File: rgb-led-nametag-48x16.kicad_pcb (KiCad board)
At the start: 4 copper layers, 84 x 28.8 mm, 109 parts, among them J1 USB_C_Receptacle_USB2.0, Q1 CJ3139K, Q10 CJ3139K, Q11 CJ3139K, Q12 CJ3139K, Q13 CJ3139K, Q14 CJ3139K, Q15 CJ3139K, Q16 CJ3139K, Q2 CJ3139K, Q3 CJ3139K, Q4 CJ3139K, Q5 CJ3139K, Q6 CJ3139K, Q7 CJ3139K, Q8 CJ3139K, Q9 CJ3139K, U1 led-panel-16x16, U10 74HC595, U11 74HC595, U12 74HC595, U13 74HC595, U14 74HC595, U15 74HC595, U16 led-panel-16x16, U17 74HC595, U18 74HC595, U19 74HC595, U2 74HC595, U20 74HC595, U21 74HC595, U22 74HC595, U23 74HC595, U24 ESP32-PICO-D4, U3 74HC595, U4 74HC595, U5 74HC595, U6 74HC595, U7 74HC595, U8 74HC595, U9 led-panel-16x16

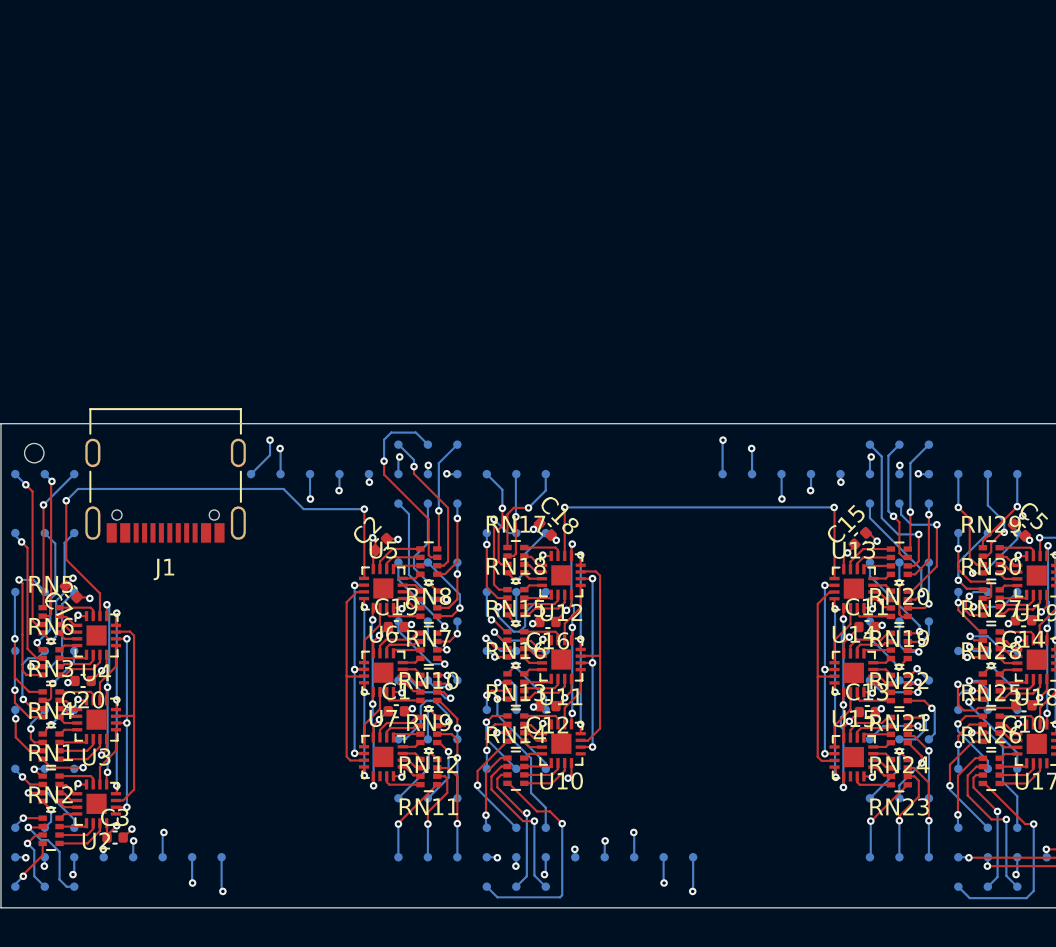
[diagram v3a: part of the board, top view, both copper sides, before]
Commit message: Add multiplexing MCU and USB
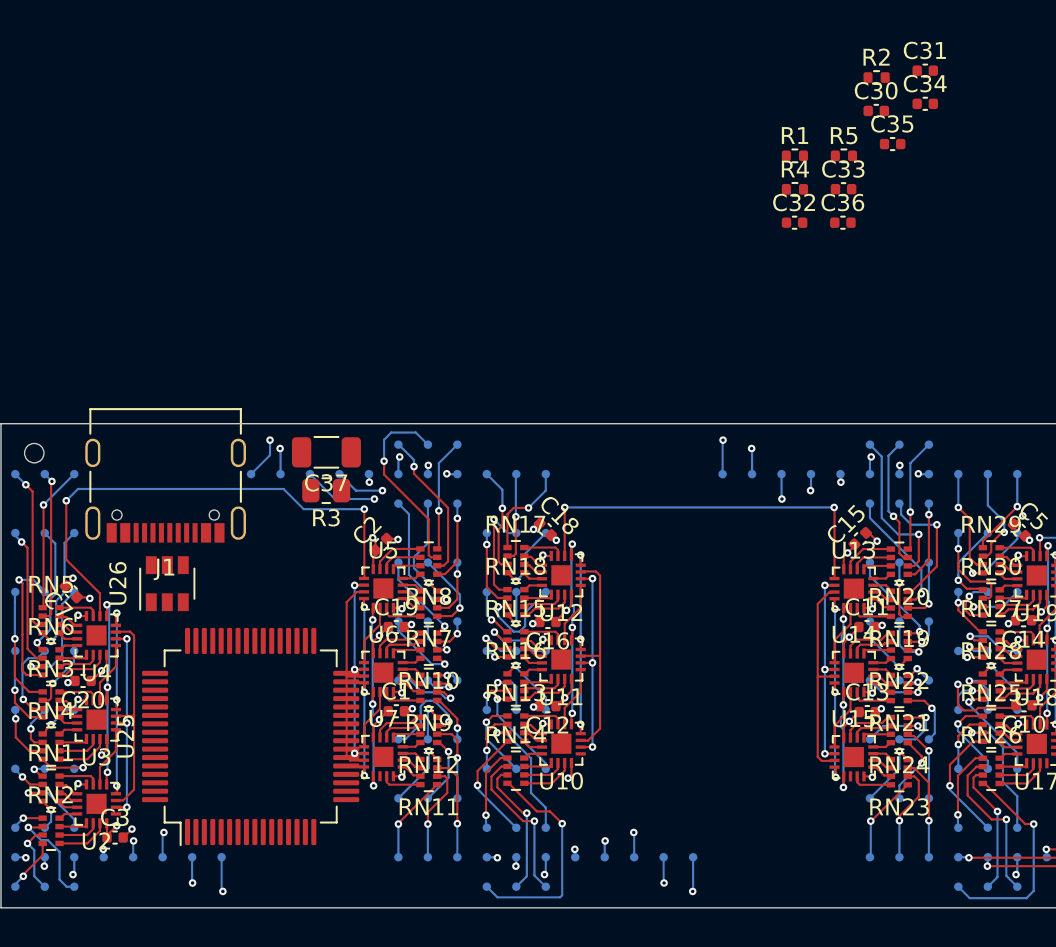
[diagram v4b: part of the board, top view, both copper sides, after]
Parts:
- added C30: 100nF, Capacitor_SMD:C_0402_1005Metric, F.Cu at (143.4, 76.2)
- added C31: 4.7uF, Capacitor_SMD:C_0402_1005Metric, F.Cu at (146.3, 73.8)
- added C32: 100nF, Capacitor_SMD:C_0402_1005Metric, F.Cu at (138.6, 82.8)
- added C33: 100nF, Capacitor_SMD:C_0402_1005Metric, F.Cu at (141.5, 80.8)
- added C34: 100nF, Capacitor_SMD:C_0402_1005Metric, F.Cu at (146.3, 75.7)
- added C35: 100nF, Capacitor_SMD:C_0402_1005Metric, F.Cu at (144.4, 78.1)
- added C36: 100nF, Capacitor_SMD:C_0402_1005Metric, F.Cu at (141.4, 82.8)
- added C37: 1nF, Capacitor_SMD:C_1206_3216Metric, F.Cu at (110.8, 96.4)
- added R1: 100k, Resistor_SMD:R_0402_1005Metric, F.Cu at (138.6, 78.8)
- added R2: 100k, Resistor_SMD:R_0402_1005Metric, F.Cu at (143.4, 74.2)
- added R3: 200k, Resistor_SMD:R_0805_2012Metric, F.Cu at (110.7, 98.7)
- added R4: 5.1k, Resistor_SMD:R_0402_1005Metric, F.Cu at (138.6, 80.8)
- added R5: 5.1k, Resistor_SMD:R_0402_1005Metric, F.Cu at (141.5, 78.8)
- added U25: STM32F722RETx, Package_QFP:LQFP-64_10x10mm_P0.5mm, F.Cu at (106.2, 113.3)
- added U26: SRV05-4, Package_TO_SOT_SMD:SOT-23-6, F.Cu at (101.3, 104.2)
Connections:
- net /Low side 1/CLK renamed /SPI2_CLK
- net /Low side 1/LATCH renamed /ROW_LATCH
- net /Low side 1/~OE renamed /ROW_~OE
- net /Low side 1/~RST renamed /ROW_~RST
- net Net-(U24-Pad17) renamed /Sheet620161B9/HSPICLK
- net Net-(U24-Pad18) renamed /Sheet620161B9/HSPIQ
- net Net-(U24-Pad20) renamed /Sheet620161B9/HSPID
- net Net-(U24-Pad21) renamed /Sheet620161B9/HSPICS
- net Net-(U24-Pad34) renamed /Sheet620161B9/VSPICS
- net Net-(U24-Pad35) renamed /Sheet620161B9/VSPICLK
- net Net-(U24-Pad36) renamed /Sheet620161B9/VSPID
- net Net-(U24-Pad38) renamed /Sheet620161B9/VSPIQ
- J1 pad A1: Net-(J1-PadA1) -> GND
- J1 pad A12: Net-(J1-PadA1) -> GND
- J1 pad A6: Net-(J1-PadA6) -> /D+
- J1 pad A7: Net-(J1-PadA7) -> /D-
- J1 pad B1: Net-(J1-PadA1) -> GND
- J1 pad B12: Net-(J1-PadA1) -> GND
- J1 pad B6: Net-(J1-PadB6) -> /D+
- J1 pad B7: Net-(J1-PadB7) -> /D-
- U10 pad 10: /Panel 2/~RST~_LOW -> /COL_~RST
- U10 pad 11: /Panel 2/CLK_LOW -> /QSPI_CLK
- U10 pad 12: /Panel 2/LATCH_LOW -> /COL_LATCH
- U10 pad 13: /Panel 2/~OE~_LOW -> /COL_~OE
- U11 pad 10: /Panel 2/~RST~_LOW -> /COL_~RST
- U11 pad 11: /Panel 2/CLK_LOW -> /QSPI_CLK
- U11 pad 12: /Panel 2/LATCH_LOW -> /COL_LATCH
- U11 pad 13: /Panel 2/~OE~_LOW -> /COL_~OE
- U12 pad 10: /Panel 2/~RST~_LOW -> /COL_~RST
- U12 pad 11: /Panel 2/CLK_LOW -> /QSPI_CLK
- U12 pad 12: /Panel 2/LATCH_LOW -> /COL_LATCH
- U12 pad 13: /Panel 2/~OE~_LOW -> /COL_~OE
- U13 pad 10: /Panel 2/~RST~_LOW -> /COL_~RST
- U13 pad 11: /Panel 2/CLK_LOW -> /QSPI_CLK
- U13 pad 12: /Panel 2/LATCH_LOW -> /COL_LATCH
- U13 pad 13: /Panel 2/~OE~_LOW -> /COL_~OE
- U14 pad 10: /Panel 2/~RST~_LOW -> /COL_~RST
- U14 pad 11: /Panel 2/CLK_LOW -> /QSPI_CLK
- U14 pad 12: /Panel 2/LATCH_LOW -> /COL_LATCH
- U14 pad 13: /Panel 2/~OE~_LOW -> /COL_~OE
- U15 pad 10: /Panel 2/~RST~_LOW -> /COL_~RST
- U15 pad 11: /Panel 2/CLK_LOW -> /QSPI_CLK
- U15 pad 12: /Panel 2/LATCH_LOW -> /COL_LATCH
- U15 pad 13: /Panel 2/~OE~_LOW -> /COL_~OE
- U15 pad 14: /Panel 2/SIN_LOW -> /QSPI_D1
- U17 pad 10: /Panel 3/~RST~_LOW -> /COL_~RST
- U17 pad 11: /Panel 3/CLK_LOW -> /QSPI_CLK
- U17 pad 12: /Panel 3/LATCH_LOW -> /COL_LATCH
- U17 pad 13: /Panel 3/~OE~_LOW -> /COL_~OE
- U18 pad 10: /Panel 3/~RST~_LOW -> /COL_~RST
- U18 pad 11: /Panel 3/CLK_LOW -> /QSPI_CLK
- U18 pad 12: /Panel 3/LATCH_LOW -> /COL_LATCH
- U18 pad 13: /Panel 3/~OE~_LOW -> /COL_~OE
- U19 pad 10: /Panel 3/~RST~_LOW -> /COL_~RST
- U19 pad 11: /Panel 3/CLK_LOW -> /QSPI_CLK
- U19 pad 12: /Panel 3/LATCH_LOW -> /COL_LATCH
- U19 pad 13: /Panel 3/~OE~_LOW -> /COL_~OE
- U2 pad 10: /Panel 1/~RST~_LOW -> /COL_~RST
- U2 pad 11: /Panel 1/CLK_LOW -> /QSPI_CLK
- U2 pad 12: /Panel 1/LATCH_LOW -> /COL_LATCH
- U2 pad 13: /Panel 1/~OE~_LOW -> /COL_~OE
- U20 pad 10: /Panel 3/~RST~_LOW -> /COL_~RST
- U20 pad 11: /Panel 3/CLK_LOW -> /QSPI_CLK
- U20 pad 12: /Panel 3/LATCH_LOW -> /COL_LATCH
- U20 pad 13: /Panel 3/~OE~_LOW -> /COL_~OE
- U21 pad 10: /Panel 3/~RST~_LOW -> /COL_~RST
- U21 pad 11: /Panel 3/CLK_LOW -> /QSPI_CLK
- U21 pad 12: /Panel 3/LATCH_LOW -> /COL_LATCH
- U21 pad 13: /Panel 3/~OE~_LOW -> /COL_~OE
- U22 pad 10: /Panel 3/~RST~_LOW -> /COL_~RST
- U22 pad 11: /Panel 3/CLK_LOW -> /QSPI_CLK
- U22 pad 12: /Panel 3/LATCH_LOW -> /COL_LATCH
- U22 pad 13: /Panel 3/~OE~_LOW -> /COL_~OE
- U22 pad 14: /Panel 3/SIN_LOW -> /QSPI_D3
- U3 pad 10: /Panel 1/~RST~_LOW -> /COL_~RST
- U3 pad 11: /Panel 1/CLK_LOW -> /QSPI_CLK
- U3 pad 12: /Panel 1/LATCH_LOW -> /COL_LATCH
- U3 pad 13: /Panel 1/~OE~_LOW -> /COL_~OE
- U4 pad 10: /Panel 1/~RST~_LOW -> /COL_~RST
- U4 pad 11: /Panel 1/CLK_LOW -> /QSPI_CLK
- U4 pad 12: /Panel 1/LATCH_LOW -> /COL_LATCH
- U4 pad 13: /Panel 1/~OE~_LOW -> /COL_~OE
- U5 pad 10: /Panel 1/~RST~_LOW -> /COL_~RST
- U5 pad 11: /Panel 1/CLK_LOW -> /QSPI_CLK
- U5 pad 12: /Panel 1/LATCH_LOW -> /COL_LATCH
- U5 pad 13: /Panel 1/~OE~_LOW -> /COL_~OE
- U6 pad 10: /Panel 1/~RST~_LOW -> /COL_~RST
- U6 pad 11: /Panel 1/CLK_LOW -> /QSPI_CLK
- U6 pad 12: /Panel 1/LATCH_LOW -> /COL_LATCH
- U6 pad 13: /Panel 1/~OE~_LOW -> /COL_~OE
- U7 pad 10: /Panel 1/~RST~_LOW -> /COL_~RST
- U7 pad 11: /Panel 1/CLK_LOW -> /QSPI_CLK
- U7 pad 12: /Panel 1/LATCH_LOW -> /COL_LATCH
- U7 pad 13: /Panel 1/~OE~_LOW -> /COL_~OE
- U7 pad 14: /Panel 1/SIN_LOW -> /QSPI_D0
- U8 pad 14: /Low side 1/SIN -> /SPI2_MOSI
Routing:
- net /QSPI_CLK: track 0.00 -> 76.6 mm
- net /COL_~OE: track 0.00 -> 73.0 mm, vias 0 -> 18
- net /COL_~RST: track 0.00 -> 70.6 mm, vias 0 -> 18
- net /COL_LATCH: track 0.00 -> 70.2 mm, vias 0 -> 18
- net /Panel 2/CLK_LOW: track 25.5 -> 0.00 mm
- net /Panel 3/CLK_LOW: track 25.5 -> 0.00 mm
- net /Panel 1/CLK_LOW: track 25.4 -> 0.00 mm
- net /Panel 2/~OE~_LOW: track 24.5 -> 0.00 mm, vias 6 -> 0
- net /Panel 3/~OE~_LOW: track 24.4 -> 0.00 mm, vias 6 -> 0
- net /Panel 1/~OE~_LOW: track 24.1 -> 0.00 mm, vias 6 -> 0
- net /Panel 2/~RST~_LOW: track 23.7 -> 0.00 mm, vias 6 -> 0
- net /Panel 1/~RST~_LOW: track 23.6 -> 0.00 mm, vias 6 -> 0
- net /Panel 2/LATCH_LOW: track 23.5 -> 0.00 mm, vias 6 -> 0
- net /Panel 1/LATCH_LOW: track 23.5 -> 0.00 mm, vias 6 -> 0
- net /Panel 3/~RST~_LOW: track 23.3 -> 0.00 mm, vias 6 -> 0
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
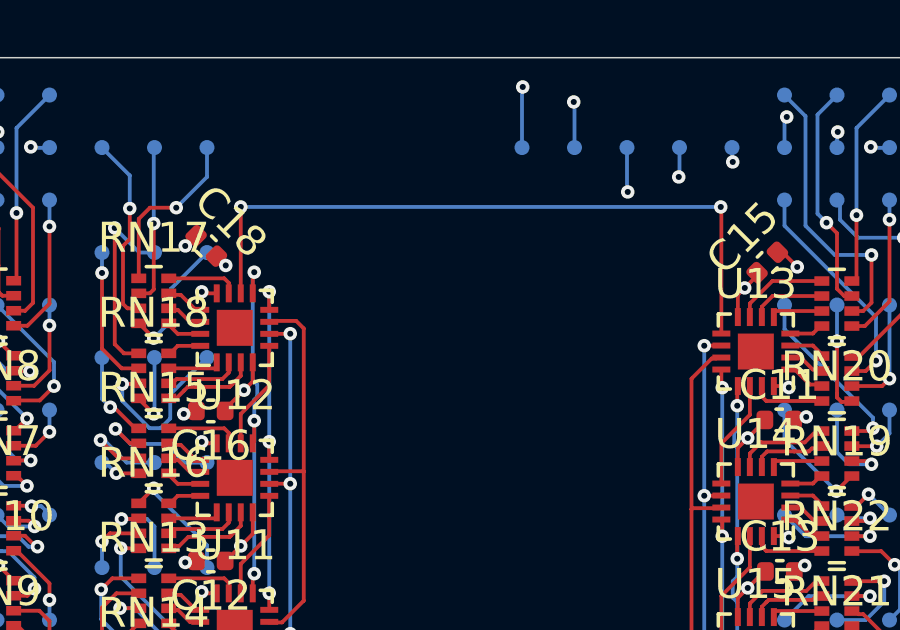
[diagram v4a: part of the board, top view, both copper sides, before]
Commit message: Add tag connect programming/debug interface
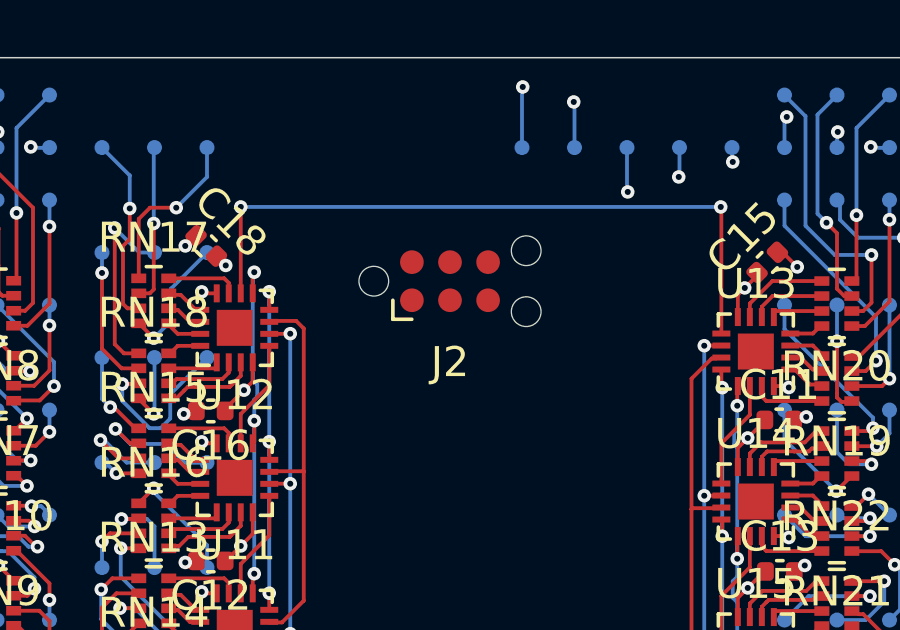
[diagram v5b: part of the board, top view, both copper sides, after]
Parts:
- added J2: TagConnect_TC2030_SWD, Connector:Tag-Connect_TC2030-IDC-NL_2x03_P1.27mm_Vertical, F.Cu at (131.9, 102.2)
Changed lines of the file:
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@@
     (tracks 2454)
     (zones 0)
-    (modules 124)
-    (nets 453)
+    (modules 125)
+    (nets 459)
   )
   (page A4)
@@
   (net 451 "Net-(U26-Pad2)")
   (net 452 "Net-(U26-Pad1)")
+  (net 453 "Net-(J2-Pad6)")
+  (net 454 "Net-(J2-Pad5)")
+  (net 455 "Net-(J2-Pad4)")
+  (net 456 "Net-(J2-Pad3)")
+  (net 457 "Net-(J2-Pad2)")
+  (net 458 "Net-(J2-Pad1)")
   (net_class Default "This is the default net class."
     (clearance 0.127)
@@
     (add_net "Net-(J1-PadB5)")
     (add_net "Net-(J1-PadB8)")
+    (add_net "Net-(J2-Pad1)")
+    (add_net "Net-(J2-Pad2)")
+    (add_net "Net-(J2-Pad3)")
+    (add_net "Net-(J2-Pad4)")
+    (add_net "Net-(J2-Pad5)")
+    (add_net "Net-(J2-Pad6)")
     (add_net "Net-(Q1-Pad1)")
     (add_net "Net-(Q10-Pad1)")
@@
     (add_net VBUS)
   )
+  (module Connector:Tag-Connect_TC2030-IDC-NL_2x03_P1.27mm_Vertical (layer F.Cu)
+    (at 131.875 102.175)
+    (descr "Tag-Connect programming header; http://www.tag-connect.com/Materials/TC2030-IDC-NL.pdf")
+    (tags "tag connect programming header pogo pins")
+    (attr virtual)
+    (fp_text reference J2 (at 0 2.7) (layer F.SilkS)
+      (effects (font (size 1 1) (thickness 0.15)))
+    )
+    (fp_text value TagConnect_TC2030_SWD (at 0 -2.3) (layer F.Fab)
+      (effects (font (size 1 1) (thickness 0.15)))
+    )
+    (fp_text user KEEPOUT (at 0 0) (layer Cmts.User)
+      (effects (font (size 0.4 0.4) (thickness 0.07)))
+    )
+    (fp_text user %R (at 0 0) (layer F.Fab)
+      (effects (font (size 1 1) (thickness 0.15)))
+    )
+    (fp_line (start -1.905 1.27) (end -1.905 0.635) (layer F.SilkS) (width 0.12))
+    (fp_line (start -1.27 1.27) (end -1.905 1.27) (layer F.SilkS) (width 0.12))
+    (fp_line (start -3.5 2) (end -3.5 -2) (layer F.CrtYd) (width 0.05))
+    (fp_line (start 3.5 2) (end -3.5 2) (layer F.CrtYd) (width 0.05))
+    (fp_line (start 3.5 -2) (end 3.5 2) (layer F.CrtYd) (width 0.05))
+    (fp_line (start -3.5 -2) (end 3.5 -2) (layer F.CrtYd) (width 0.05))
+    (fp_line (start -1.27 0.635) (end -1.27 -0.635) (layer Dwgs.User) (width 0.1))
+    (fp_line (start 1.27 0.635) (end -1.27 0.635) (layer Dwgs.User) (width 0.1))
+    (fp_line (start 1.27 -0.635) (end 1.27 0.635) (layer Dwgs.User) (width 0.1))
+    (fp_line (start -1.27 -0.635) (end 1.27 -0.635) (layer Dwgs.User) (width 0.1))
+    (fp_line (start -1.27 0.635) (end 0 -0.635) (layer Dwgs.User) (width 0.1))
+    (fp_line (start -1.27 0) (end -0.635 -0.635) (layer Dwgs.User) (width 0.1))
+    (fp_line (start -0.635 0.635) (end 0.635 -0.635) (layer Dwgs.User) (width 0.1))
+    (fp_line (start 0 0.635) (end 1.27 -0.635) (layer Dwgs.User) (width 0.1))
+    (fp_line (start 0.635 0.635) (end 1.27 0) (layer Dwgs.User) (width 0.1))
+    (pad 6 connect circle (at 1.27 -0.635) (size 0.7874 0.7874) (layers F.Cu F.Mask)
+      (net 453 "Net-(J2-Pad6)"))
+    (pad 5 connect circle (at 1.27 0.635) (size 0.7874 0.7874) (layers F.Cu F.Mask)
+      (net 454 "Net-(J2-Pad5)"))
+    (pad 4 connect circle (at 0 -0.635) (size 0.7874 0.7874) (layers F.Cu F.Mask)
+      (net 455 "Net-(J2-Pad4)"))
+    (pad 3 connect circle (at 0 0.635) (size 0.7874 0.7874) (layers F.Cu F.Mask)
+      (net 456 "Net-(J2-Pad3)"))
+    (pad 2 connect circle (at -1.27 -0.635) (size 0.7874 0.7874) (layers F.Cu F.Mask)
+      (net 457 "Net-(J2-Pad2)"))
+    (pad 1 connect circle (at -1.27 0.635) (size 0.7874 0.7874) (layers F.Cu F.Mask)
+      (net 458 "Net-(J2-Pad1)"))
+    (pad "" np_thru_hole circle (at -2.54 0) (size 0.9906 0.9906) (drill 0.9906) (layers *.Cu *.Mask))
+    (pad "" np_thru_hole circle (at 2.54 1.016) (size 0.9906 0.9906) (drill 0.9906) (layers *.Cu *.Mask))
+    (pad "" np_thru_hole circle (at 2.54 -1.016) (size 0.9906 0.9906) (drill 0.9906) (layers *.Cu *.Mask))
+  )
   (module Package_TO_SOT_SMD:SOT-23-6 (layer F.Cu)

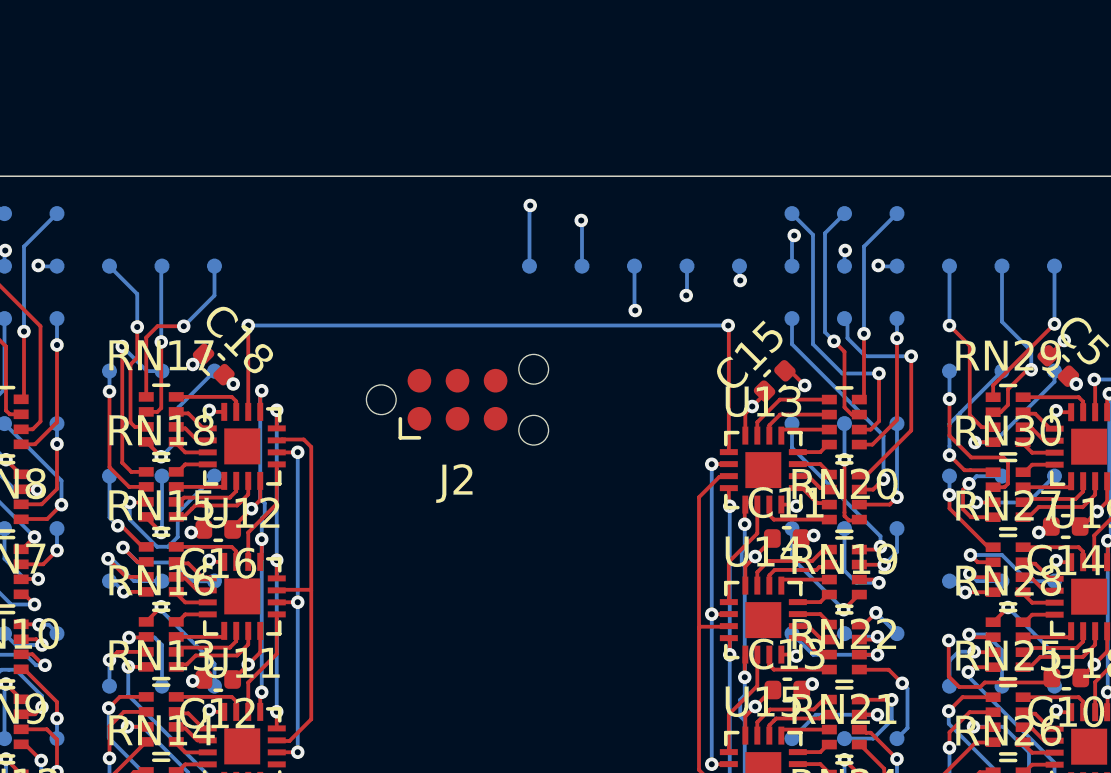
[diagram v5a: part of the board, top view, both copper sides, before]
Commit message: Add mounting pad for safety pin
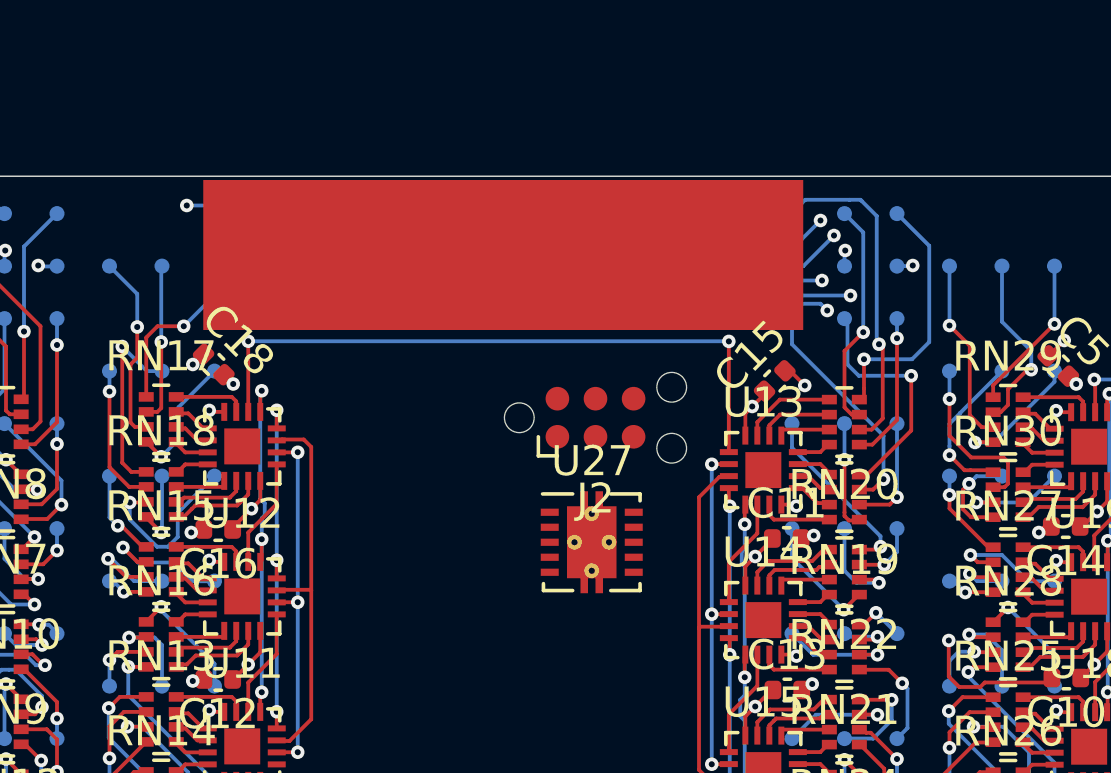
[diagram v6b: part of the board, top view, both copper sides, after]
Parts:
- added H3: MountingPad, MountingPad:MountingPad_20x5mm, F.Cu at (133.4, 97.3)
- added U27: TPS63001, Package_SON:Texas_DRC0010J_ThermalVias, F.Cu at (136.3, 106.9)
- moved J2 4.64 mm to (136.5, 102.8)
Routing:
- net /A9: track 71.5 -> 81.7 mm
- net /A10: track 70.4 -> 77.5 mm
- net /A11: track 65.8 -> 71.3 mm
- net /A12: track 59.7 -> 64.5 mm
- net /A13: track 60.0 -> 62.3 mm
- net /Panel 2/B16: track 6.61 -> 8.44 mm
- net /Panel 2/R16: track 9.61 -> 11.0 mm
- net /Panel 2/sheet61A6C351/SIN: track 23.1 -> 22.1 mm
- net /A14: track 62.8 -> 63.6 mm
